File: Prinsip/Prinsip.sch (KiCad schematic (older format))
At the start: 21 parts

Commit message: One element
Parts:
- removed U? (x7): 7451N, symbol Prinsip:7451N
- removed U? (x7): 7426N, symbol Prinsip:7426N
- added U? (x2): 7426N, symbol Prinsip:7426N
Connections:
- wire segments 0 -> 9
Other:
- moved on the sheet: U?A

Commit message: Optimized
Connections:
- wire segments 9 -> 11
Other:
- moved on the sheet: U?A
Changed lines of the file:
@@
 L Prinsip:7420N U?
 U 1 1 61669E61
-P 8100 3100
-F 0 "U?" H 8075 3566 50  0000 C CNN
-F 1 "7420N" H 8075 3475 50  0000 C CNN
-F 2 "" H 8100 3250 50  0001 C CNN
-F 3 "" H 8100 3250 50  0001 C CNN
-	1    8100 3100
+P 10750 3050
+F 0 "U?" H 10725 3516 50  0000 C CNN
+F 1 "7420N" H 10725 3425 50  0000 C CNN
+F 2 "" H 10750 3200 50  0001 C CNN
+F 3 "" H 10750 3200 50  0001 C CNN
+	1    10750 3050
 	1    0    0    -1
 $EndComp
@@
 L Prinsip:7420N U?
 U 1 1 6166CDF9
-P 8100 7000
-F 0 "U?" H 8075 7466 50  0000 C CNN
-F 1 "7420N" H 8075 7375 50  0000 C CNN
-F 2 "" H 8100 7150 50  0001 C CNN
-F 3 "" H 8100 7150 50  0001 C CNN
-	1    8100 7000
+P 10750 6950
+F 0 "U?" H 10725 7416 50  0000 C CNN
+F 1 "7420N" H 10725 7325 50  0000 C CNN
+F 2 "" H 10750 7100 50  0001 C CNN
+F 3 "" H 10750 7100 50  0001 C CNN
+	1    10750 6950
 	1    0    0    -1
 $EndComp
@@
 L Prinsip:7426N U?
 U 1 1 6166FCF7
-P 9450 3950
-F 0 "U?" H 9450 4416 50  0000 C CNN
-F 1 "7426N" H 9450 4325 50  0000 C CNN
-F 2 "" H 9450 4100 50  0001 C CNN
-F 3 "" H 9450 4100 50  0001 C CNN
-	1    9450 3950
+P 12100 3900
+F 0 "U?" H 12100 4366 50  0000 C CNN
+F 1 "7426N" H 12100 4275 50  0000 C CNN
+F 2 "" H 12100 4050 50  0001 C CNN
+F 3 "" H 12100 4050 50  0001 C CNN
+	1    12100 3900
 	1    0    0    -1
 $EndComp
@@
 L Prinsip:7426N U?
 U 1 1 61671269
-P 9450 5900
-F 0 "U?" H 9450 6366 50  0000 C CNN
-F 1 "7426N" H 9450 6275 50  0000 C CNN
-F 2 "" H 9450 6050 50  0001 C CNN
-F 3 "" H 9450 6050 50  0001 C CNN
-	1    9450 5900
+P 12100 5850
+F 0 "U?" H 12100 6316 50  0000 C CNN
+F 1 "7426N" H 12100 6225 50  0000 C CNN
+F 2 "" H 12100 6000 50  0001 C CNN
+F 3 "" H 12100 6000 50  0001 C CNN
+	1    12100 5850
 	1    0    0    -1
 $EndComp
@@
 L Prinsip:7426N U?
 U 1 1 61671C84
-P 10950 4900
-F 0 "U?" H 10950 5366 50  0000 C CNN
-F 1 "7426N" H 10950 5275 50  0000 C CNN
-F 2 "" H 10950 5050 50  0001 C CNN
-F 3 "" H 10950 5050 50  0001 C CNN
-	1    10950 4900
-	1    0    0    -1
-$EndComp
-$Comp
-L Prinsip:7426N U?
-U 1 1 6166AF0B
-P 3500 3000
-F 0 "U?" H 3500 3466 50  0000 C CNN
-F 1 "7426N" H 3500 3375 50  0000 C CNN
-F 2 "" H 3500 3150 50  0001 C CNN
-F 3 "" H 3500 3150 50  0001 C CNN
-	1    3500 3000
+P 13600 4850
+F 0 "U?" H 13600 5316 50  0000 C CNN
+F 1 "7426N" H 13600 5225 50  0000 C CNN
+F 2 "" H 13600 5000 50  0001 C CNN
+F 3 "" H 13600 5000 50  0001 C CNN
+	1    13600 4850
 	1    0    0    -1
 $EndComp
@@
 L Prinsip:7426N U?
 U 1 1 6166A9DA
-P 3500 2200
-F 0 "U?" H 3500 2666 50  0000 C CNN
-F 1 "7426N" H 3500 2575 50  0000 C CNN
-F 2 "" H 3500 2350 50  0001 C CNN
-F 3 "" H 3500 2350 50  0001 C CNN
-	1    3500 2200
+P 2350 1700
+F 0 "U?" H 2350 2166 50  0000 C CNN
+F 1 "7426N" H 2350 2075 50  0000 C CNN
+F 2 "" H 2350 1850 50  0001 C CNN
+F 3 "" H 2350 1850 50  0001 C CNN
+	1    2350 1700
 	1    0    0    -1
 $EndComp
 Wire Wire Line
-	4400 1700 4000 1700
-Wire Wire Line
-	4000 1700 4000 2200
-Wire Wire Line
 	4400 1800 4100 1800
-Wire Wire Line
-	4100 1800 4100 3000
-Wire Wire Line
-	4100 3000 4000 3000
 $Comp
 L Prinsip:7426N U?
@@
 Wire Wire Line
 	5650 1650 5650 1750
+Wire Wire Line
+	4400 1500 2600 1500
+Wire Wire Line
+	2850 1700 4400 1700
+Wire Wire Line
+	4100 2800 4000 2800
+$Comp
+L Prinsip:7426N U?
+U 1 1 6166AF0B
+P 3500 2800
+F 0 "U?" H 3500 3266 50  0000 C CNN
+F 1 "7426N" H 3500 3175 50  0000 C CNN
+F 2 "" H 3500 2950 50  0001 C CNN
+F 3 "" H 3500 2950 50  0001 C CNN
+	1    3500 2800
+	1    0    0    -1
+$EndComp
+Wire Wire Line
+	3000 2700 3000 2800
+Wire Wire Line
+	2800 2800 3000 2800
+Connection ~ 3000 2800
+Wire Wire Line
+	3000 2800 3000 2900
 $EndSCHEMATC

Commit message: 7451 placement
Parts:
- added U? (x7): 7451N, symbol Prinsip:7451N
- added U? (x21): 7426N, symbol Prinsip:7426N
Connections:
- wire segments 11 -> 136
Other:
- moved on the sheet: U?A

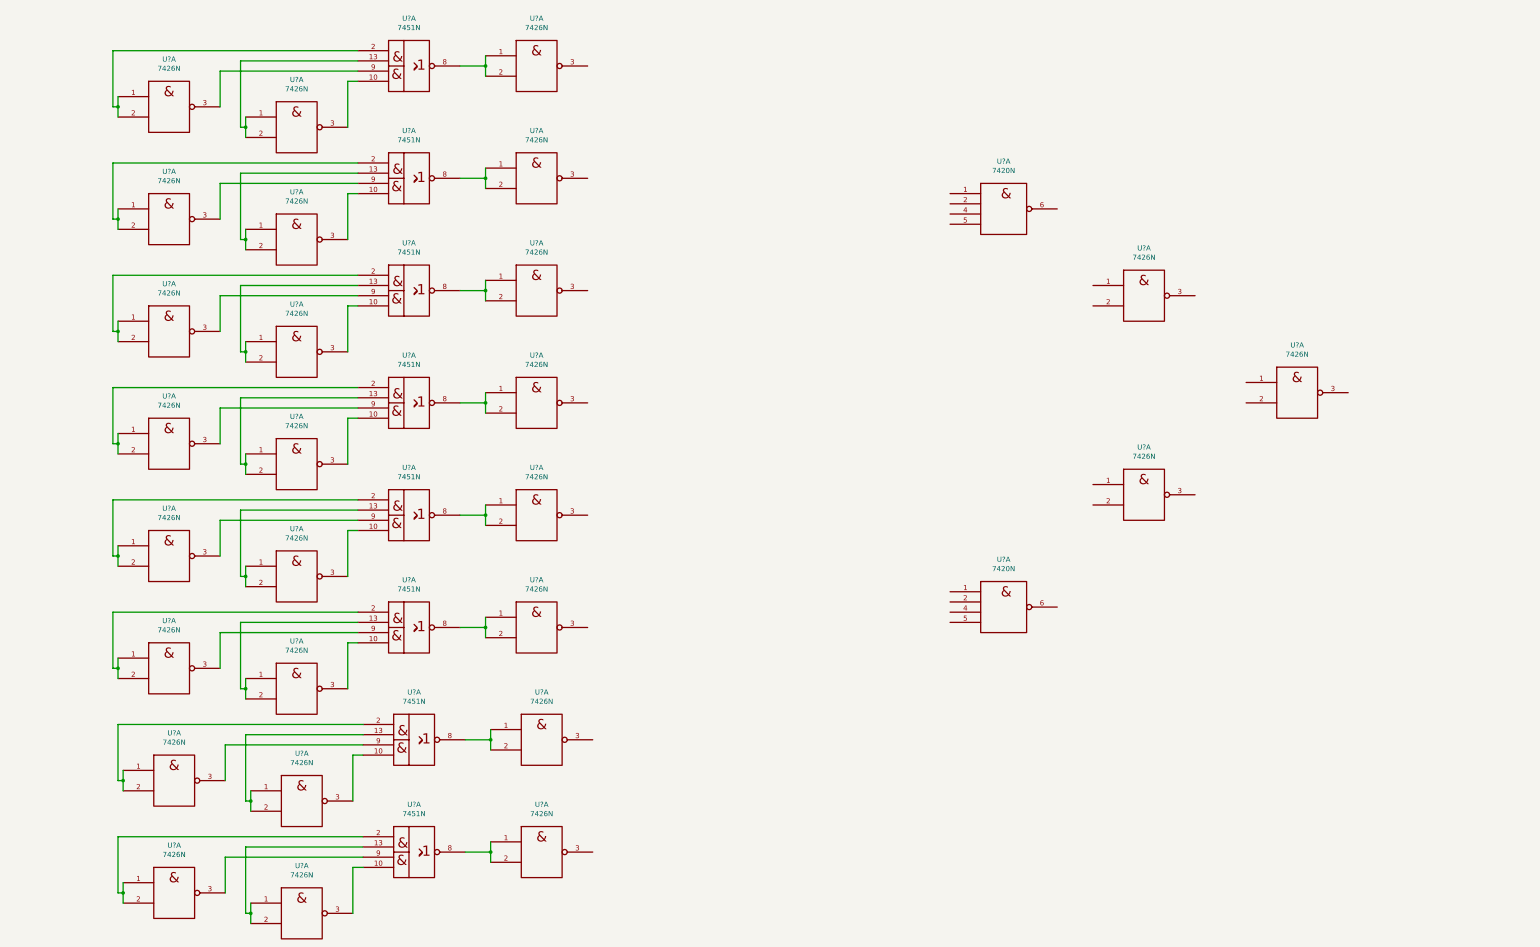
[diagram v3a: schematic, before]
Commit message: 7426N placement
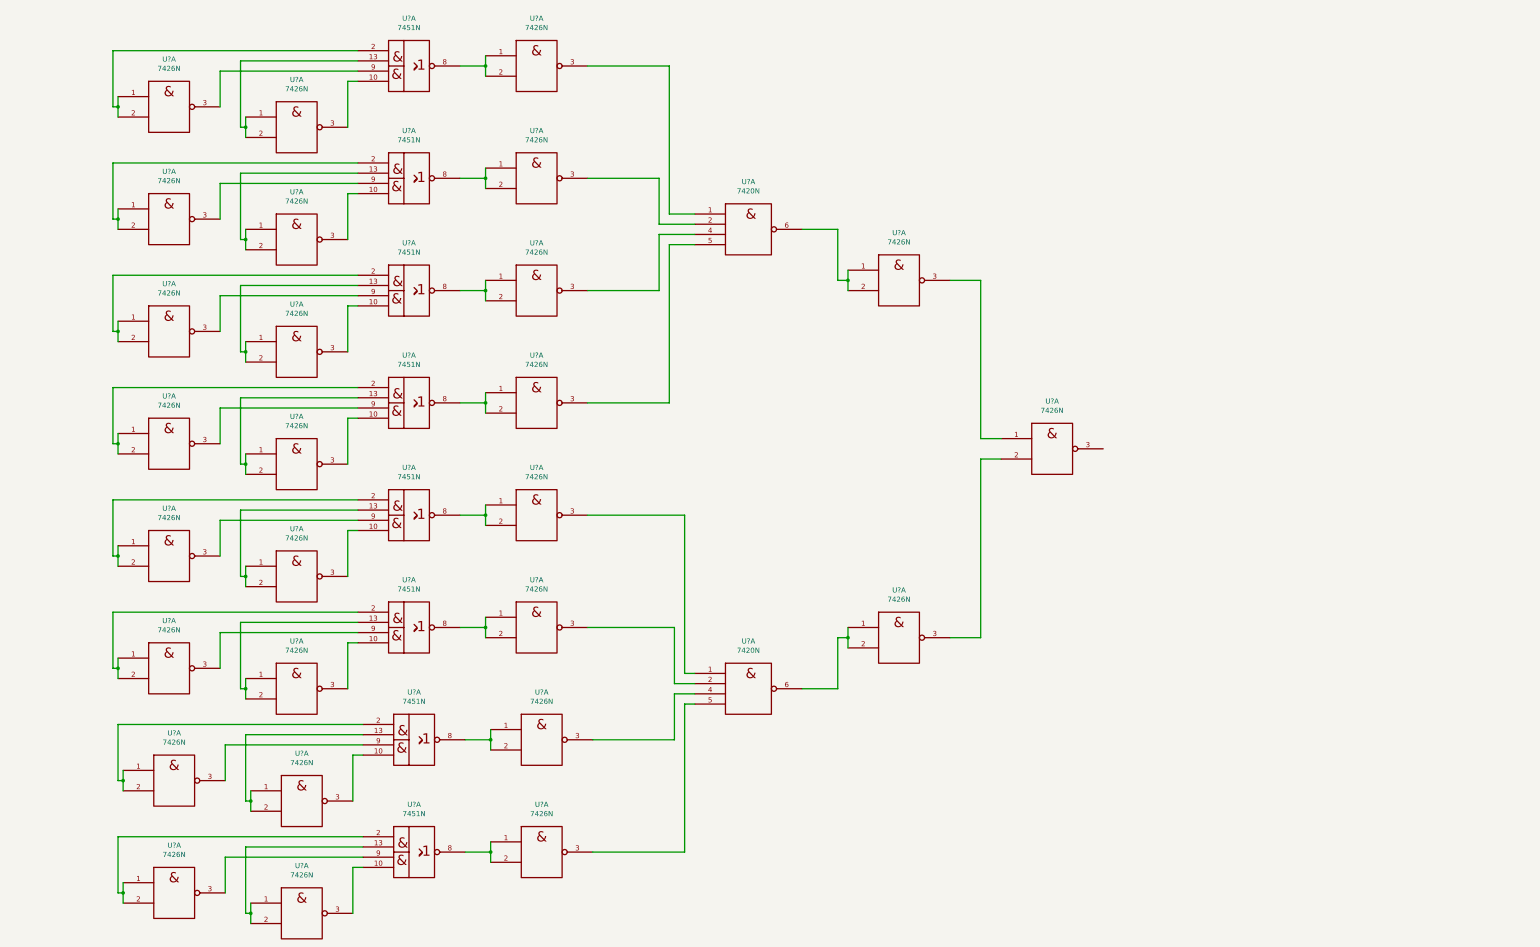
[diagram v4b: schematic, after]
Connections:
- net at U?.3: now also U?.1 (x2)
- net at U?.2: now also U?.3 (x2)
- net at U?.4: now also U?.3 (x2)
- net at U?.5: now also U?.3 (x2)
- net at U?.6: now also U?.1, U?.2 (x2)
- net at U?.1: now also U?.3
- net at U?.3: now also U?.2
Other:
- moved on the sheet: U?A
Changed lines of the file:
@@
 L Prinsip:7420N U?
 U 1 1 61669E61
-P 10750 3050
-F 0 "U?" H 10725 3516 50  0000 C CNN
-F 1 "7420N" H 10725 3425 50  0000 C CNN
-F 2 "" H 10750 3200 50  0001 C CNN
-F 3 "" H 10750 3200 50  0001 C CNN
-	1    10750 3050
+P 8250 3250
+F 0 "U?" H 8225 3716 50  0000 C CNN
+F 1 "7420N" H 8225 3625 50  0000 C CNN
+F 2 "" H 8250 3400 50  0001 C CNN
+F 3 "" H 8250 3400 50  0001 C CNN
+	1    8250 3250
 	1    0    0    -1
 $EndComp
@@
 L Prinsip:7420N U?
 U 1 1 6166CDF9
-P 10750 6950
-F 0 "U?" H 10725 7416 50  0000 C CNN
-F 1 "7420N" H 10725 7325 50  0000 C CNN
-F 2 "" H 10750 7100 50  0001 C CNN
-F 3 "" H 10750 7100 50  0001 C CNN
-	1    10750 6950
+P 8250 7750
+F 0 "U?" H 8225 8216 50  0000 C CNN
+F 1 "7420N" H 8225 8125 50  0000 C CNN
+F 2 "" H 8250 7900 50  0001 C CNN
+F 3 "" H 8250 7900 50  0001 C CNN
+	1    8250 7750
 	1    0    0    -1
 $EndComp
@@
 L Prinsip:7426N U?
 U 1 1 6166FCF7
-P 12100 3900
-F 0 "U?" H 12100 4366 50  0000 C CNN
-F 1 "7426N" H 12100 4275 50  0000 C CNN
-F 2 "" H 12100 4050 50  0001 C CNN
-F 3 "" H 12100 4050 50  0001 C CNN
-	1    12100 3900
+P 9700 3750
+F 0 "U?" H 9700 4216 50  0000 C CNN
+F 1 "7426N" H 9700 4125 50  0000 C CNN
+F 2 "" H 9700 3900 50  0001 C CNN
+F 3 "" H 9700 3900 50  0001 C CNN
+	1    9700 3750
 	1    0    0    -1
 $EndComp
@@
 L Prinsip:7426N U?
 U 1 1 61671269
-P 12100 5850
-F 0 "U?" H 12100 6316 50  0000 C CNN
-F 1 "7426N" H 12100 6225 50  0000 C CNN
-F 2 "" H 12100 6000 50  0001 C CNN
-F 3 "" H 12100 6000 50  0001 C CNN
-	1    12100 5850
+P 9700 7250
+F 0 "U?" H 9700 7716 50  0000 C CNN
+F 1 "7426N" H 9700 7625 50  0000 C CNN
+F 2 "" H 9700 7400 50  0001 C CNN
+F 3 "" H 9700 7400 50  0001 C CNN
+	1    9700 7250
 	1    0    0    -1
 $EndComp
@@
 L Prinsip:7426N U?
 U 1 1 61671C84
-P 13600 4850
-F 0 "U?" H 13600 5316 50  0000 C CNN
-F 1 "7426N" H 13600 5225 50  0000 C CNN
-F 2 "" H 13600 5000 50  0001 C CNN
-F 3 "" H 13600 5000 50  0001 C CNN
-	1    13600 4850
+P 11200 5400
+F 0 "U?" H 11200 5866 50  0000 C CNN
+F 1 "7426N" H 11200 5775 50  0000 C CNN
+F 2 "" H 11200 5550 50  0001 C CNN
+F 3 "" H 11200 5550 50  0001 C CNN
+	1    11200 5400
 	1    0    0    -1
 $EndComp
@@
 Wire Wire Line
 	3350 9950 3350 10050
+Wire Wire Line
+	6650 1650 7450 1650
+Wire Wire Line
+	7450 1650 7450 3100
+Wire Wire Line
+	7450 3100 7700 3100
+Wire Wire Line
+	6650 2750 7350 2750
+Wire Wire Line
+	7350 2750 7350 3200
+Wire Wire Line
+	7350 3200 7700 3200
+Wire Wire Line
+	6650 3850 7350 3850
+Wire Wire Line
+	7350 3850 7350 3300
+Wire Wire Line
+	7350 3300 7700 3300
+Wire Wire Line
+	7700 3400 7450 3400
+Wire Wire Line
+	7450 3400 7450 4950
+Wire Wire Line
+	7450 4950 6650 4950
+Wire Wire Line
+	6650 6050 7600 6050
+Wire Wire Line
+	7600 6050 7600 7600
+Wire Wire Line
+	7600 7600 7700 7600
+Wire Wire Line
+	6650 7150 7500 7150
+Wire Wire Line
+	7500 7150 7500 7700
+Wire Wire Line
+	7500 7700 7700 7700
+Wire Wire Line
+	6700 8250 7500 8250
+Wire Wire Line
+	7500 8250 7500 7800
+Wire Wire Line
+	7500 7800 7700 7800
+Wire Wire Line
+	6700 9350 7600 9350
+Wire Wire Line
+	7600 9350 7600 7900
+Wire Wire Line
+	7600 7900 7700 7900
+Wire Wire Line
+	9200 7150 9200 7250
+Wire Wire Line
+	8750 7750 9100 7750
+Wire Wire Line
+	9100 7750 9100 7250
+Wire Wire Line
+	9100 7250 9200 7250
+Connection ~ 9200 7250
+Wire Wire Line
+	9200 7250 9200 7350
+Wire Wire Line
+	9200 3650 9200 3750
+Wire Wire Line
+	8750 3250 9100 3250
+Wire Wire Line
+	9100 3250 9100 3750
+Wire Wire Line
+	9100 3750 9200 3750
+Connection ~ 9200 3750
+Wire Wire Line
+	9200 3750 9200 3850
+Wire Wire Line
+	10200 3750 10500 3750
+Wire Wire Line
+	10200 7250 10500 7250
+Wire Wire Line
+	10500 3750 10500 5300
+Wire Wire Line
+	10500 5300 10700 5300
+Wire Wire Line
+	10500 7250 10500 5500
+Wire Wire Line
+	10500 5500 10700 5500
 $EndSCHEMATC

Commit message: General alignment
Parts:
- removed U?: 7420N, symbol Prinsip:7420N
- added U?: 7420N, symbol Prinsip:7420N
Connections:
- net Gnd: now also U?.7 (Gnd)
- net Vcc: now also U?.14 (Vcc)
- net at U?.3: now also U?.1
- net at U?.3: now also U?.2
- net at U?.3: now also U?.4
- net at U?.3: now also U?.5
- net at U?.1, U?.2: now also U?.6
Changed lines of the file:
@@
-$Comp
-L Prinsip:7420N U?
-U 1 1 61669E61
-P 8250 3250
-F 0 "U?" H 8225 3716 50  0000 C CNN
-F 1 "7420N" H 8225 3625 50  0000 C CNN
-F 2 "" H 8250 3400 50  0001 C CNN
-F 3 "" H 8250 3400 50  0001 C CNN
-	1    8250 3250
-	1    0    0    -1
-$EndComp
 $Comp
 L Prinsip:7420N U?
@@
 $Comp
 L Prinsip:7426N U?
-U 1 1 6166FCF7
-P 9700 3750
-F 0 "U?" H 9700 4216 50  0000 C CNN
-F 1 "7426N" H 9700 4125 50  0000 C CNN
-F 2 "" H 9700 3900 50  0001 C CNN
-F 3 "" H 9700 3900 50  0001 C CNN
-	1    9700 3750
-	1    0    0    -1
-$EndComp
-$Comp
-L Prinsip:7426N U?
 U 1 1 61671269
 P 9700 7250
@@
 F 3 "" H 11200 5550 50  0001 C CNN
 	1    11200 5400
-	1    0    0    -1
-$EndComp
-$Comp
-L Prinsip:7426N U?
-U 1 1 61665BB4
-P 6150 1650
-F 0 "U?" H 6150 2116 50  0000 C CNN
-F 1 "7426N" H 6150 2025 50  0000 C CNN
-F 2 "" H 6150 1800 50  0001 C CNN
-F 3 "" H 6150 1800 50  0001 C CNN
-	1    6150 1650
 	1    0    0    -1
 $EndComp
@@
 	1    0    0    -1
 $EndComp
-$Comp
-L Prinsip:7426N U?
-U 1 1 61672D4B
-P 6150 2750
-F 0 "U?" H 6150 3216 50  0000 C CNN
-F 1 "7426N" H 6150 3125 50  0000 C CNN
-F 2 "" H 6150 2900 50  0001 C CNN
-F 3 "" H 6150 2900 50  0001 C CNN
-	1    6150 2750
-	1    0    0    -1
-$EndComp
 Wire Wire Line
 	5650 2650 5650 2750
@@
 	1    0    0    -1
 $EndComp
-$Comp
-L Prinsip:7426N U?
-U 1 1 61675E65
-P 6150 3850
-F 0 "U?" H 6150 4316 50  0000 C CNN
-F 1 "7426N" H 6150 4225 50  0000 C CNN
-F 2 "" H 6150 4000 50  0001 C CNN
-F 3 "" H 6150 4000 50  0001 C CNN
-	1    6150 3850
-	1    0    0    -1
-$EndComp
 Wire Wire Line
 	5650 3750 5650 3850
@@
 	1    0    0    -1
 $EndComp
-$Comp
-L Prinsip:7426N U?
-U 1 1 61684585
-P 6150 4950
-F 0 "U?" H 6150 5416 50  0000 C CNN
-F 1 "7426N" H 6150 5325 50  0000 C CNN
-F 2 "" H 6150 5100 50  0001 C CNN
-F 3 "" H 6150 5100 50  0001 C CNN
-	1    6150 4950
-	1    0    0    -1
-$EndComp
 Wire Wire Line
 	5650 4850 5650 4950
@@
 	3350 9950 3350 10050
 Wire Wire Line
-	6650 1650 7450 1650
-Wire Wire Line
-	7450 1650 7450 3100
-Wire Wire Line
-	7450 3100 7700 3100
-Wire Wire Line
-	6650 2750 7350 2750
-Wire Wire Line
-	7350 2750 7350 3200
-Wire Wire Line
-	7350 3200 7700 3200
-Wire Wire Line
-	6650 3850 7350 3850
-Wire Wire Line
-	7350 3850 7350 3300
-Wire Wire Line
-	7350 3300 7700 3300
-Wire Wire Line
-	7700 3400 7450 3400
-Wire Wire Line
-	7450 3400 7450 4950
-Wire Wire Line
-	7450 4950 6650 4950
-Wire Wire Line
-	6650 6050 7600 6050
-Wire Wire Line
-	7600 6050 7600 7600
-Wire Wire Line
-	7600 7600 7700 7600
-Wire Wire Line
-	6650 7150 7500 7150
-Wire Wire Line
-	7500 7150 7500 7700
-Wire Wire Line
-	7500 7700 7700 7700
-Wire Wire Line
-	6700 8250 7500 8250
-Wire Wire Line
-	7500 8250 7500 7800
-Wire Wire Line
-	7500 7800 7700 7800
-Wire Wire Line
-	6700 9350 7600 9350
-Wire Wire Line
-	7600 9350 7600 7900
-Wire Wire Line
-	7600 7900 7700 7900
+	7500 9350 7500 7900
+Wire Wire Line
+	10200 3750 10500 3750
+Wire Wire Line
+	10200 7250 10500 7250
+Wire Wire Line
+	10500 3750 10500 5300
+Wire Wire Line
+	10500 5300 10700 5300
+Wire Wire Line
+	10500 7250 10500 5500
+Wire Wire Line
+	10500 5500 10700 5500
+Wire Wire Line
+	6700 9350 7500 9350
+Wire Wire Line
+	7500 7900 7700 7900
+Wire Wire Line
+	7000 7800 7000 8250
+Wire Wire Line
+	7000 8250 6700 8250
+Wire Wire Line
+	7000 7800 7700 7800
+Wire Wire Line
+	7500 7600 7700 7600
+Wire Wire Line
+	6650 6050 7500 6050
+Wire Wire Line
+	7500 6050 7500 7600
+Wire Wire Line
+	7700 7700 7000 7700
+Wire Wire Line
+	7000 7700 7000 7150
+Wire Wire Line
+	7000 7150 6650 7150
+$Comp
+L Prinsip:7426N U?
+U 1 1 61684585
+P 6150 4950
+F 0 "U?" H 6150 5416 50  0000 C CNN
+F 1 "7426N" H 6150 5325 50  0000 C CNN
+F 2 "" H 6150 5100 50  0001 C CNN
+F 3 "" H 6150 5100 50  0001 C CNN
+	1    6150 4950
+	1    0    0    -1
+$EndComp
+$Comp
+L Prinsip:7426N U?
+U 1 1 61675E65
+P 6150 3850
+F 0 "U?" H 6150 4316 50  0000 C CNN
+F 1 "7426N" H 6150 4225 50  0000 C CNN
+F 2 "" H 6150 4000 50  0001 C CNN
+F 3 "" H 6150 4000 50  0001 C CNN
+	1    6150 3850
+	1    0    0    -1
+$EndComp
+$Comp
+L Prinsip:7426N U?
+U 1 1 61672D4B
+P 6150 2750
+F 0 "U?" H 6150 3216 50  0000 C CNN
+F 1 "7426N" H 6150 3125 50  0000 C CNN
+F 2 "" H 6150 2900 50  0001 C CNN
+F 3 "" H 6150 2900 50  0001 C CNN
+	1    6150 2750
+	1    0    0    -1
+$EndComp
+$Comp
+L Prinsip:7426N U?
+U 1 1 61665BB4
+P 6150 1650
+F 0 "U?" H 6150 2116 50  0000 C CNN
+F 1 "7426N" H 6150 2025 50  0000 C CNN
+F 2 "" H 6150 1800 50  0001 C CNN
+F 3 "" H 6150 1800 50  0001 C CNN
+	1    6150 1650
+	1    0    0    -1
+$EndComp
+$Comp
+L Prinsip:7420N U?
+U 1 1 61810D02
+P 8250 3350
+F 0 "U?" H 8225 3816 50  0000 C CNN
+F 1 "7420N" H 8225 3725 50  0000 C CNN
+F 2 "" H 8250 3500 50  0001 C CNN
+F 3 "" H 8250 3500 50  0001 C CNN
+	1    8250 3350
+	1    0    0    -1
+$EndComp
+Wire Wire Line
+	7500 4950 7500 3500
+Wire Wire Line
+	7500 3500 7700 3500
+Wire Wire Line
+	7000 3400 7000 3850
+Wire Wire Line
+	7000 3400 7700 3400
+Wire Wire Line
+	7500 3200 7700 3200
+Wire Wire Line
+	6650 1650 7500 1650
+Wire Wire Line
+	7500 1650 7500 3200
+Wire Wire Line
+	7700 3300 7000 3300
+Wire Wire Line
+	7000 3300 7000 2750
+Wire Wire Line
+	7000 2750 6650 2750
+$Comp
+L Prinsip:7426N U?
+U 1 1 6166FCF7
+P 9700 3750
+F 0 "U?" H 9700 4216 50  0000 C CNN
+F 1 "7426N" H 9700 4125 50  0000 C CNN
+F 2 "" H 9700 3900 50  0001 C CNN
+F 3 "" H 9700 3900 50  0001 C CNN
+	1    9700 3750
+	1    0    0    -1
+$EndComp
+Wire Wire Line
+	9200 3650 9200 3750
+Wire Wire Line
+	8750 3350 9000 3350
+Wire Wire Line
+	9000 3350 9000 3750
+Wire Wire Line
+	9000 3750 9200 3750
+Connection ~ 9200 3750
+Wire Wire Line
+	9200 3750 9200 3850
 Wire Wire Line
 	9200 7150 9200 7250
 Wire Wire Line
-	8750 7750 9100 7750
-Wire Wire Line
-	9100 7750 9100 7250
-Wire Wire Line
-	9100 7250 9200 7250
+	8750 7750 9000 7750
+Wire Wire Line
+	9000 7750 9000 7250
+Wire Wire Line
+	9000 7250 9200 7250
 Connection ~ 9200 7250
 Wire Wire Line
 	9200 7250 9200 7350
 Wire Wire Line
-	9200 3650 9200 3750
-Wire Wire Line
-	8750 3250 9100 3250
-Wire Wire Line
-	9100 3250 9100 3750
-Wire Wire Line
-	9100 3750 9200 3750
-Connection ~ 9200 3750
-Wire Wire Line
-	9200 3750 9200 3850
-Wire Wire Line
-	10200 3750 10500 3750
-Wire Wire Line
-	10200 7250 10500 7250
-Wire Wire Line
-	10500 3750 10500 5300
-Wire Wire Line
-	10500 5300 10700 5300
-Wire Wire Line
-	10500 7250 10500 5500
-Wire Wire Line
-	10500 5500 10700 5500
+	6650 3850 7000 3850
+Wire Wire Line
+	6650 4950 7500 4950
 $EndSCHEMATC

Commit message: Updated
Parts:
- added SW?: SW_DIP_x08, symbol Switch:SW_DIP_x08
- added U?: DAC, symbol Prinsip:DAC
- added U?: 74199N, symbol Prinsip:74199N
- added U?: COUNTER, symbol Prinsip:COUNTER
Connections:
- net CT: now reaches U?.1, U?.13, U?.2
- net CT: now also U?.~ (~LD), U?.~ (~LOAD)
- net at U?.1, U?.2, U?.2: now also SW?.16
- net at U?.3: now also U?.~ (~LOAD)
- net CT1: now reaches U?.1, U?.13, U?.2
- net CT1: now also U?.~ (~LD), U?.~ (~LOAD)
- net at U?.1, U?.2, U?.2: now also SW?.15
- net CT2: now reaches U?.1, U?.13, U?.2
- net CT2: now also U?.~ (~LD), U?.~ (~LOAD)
- net at U?.1, U?.2, U?.2: now also SW?.14
- net CT3: now reaches U?.1, U?.13, U?.2
- net CT3: now also U?.~ (~LD), U?.~ (~LOAD)
- net at U?.1, U?.2, U?.2: now also SW?.13
- net CT4: now reaches U?.1, U?.13, U?.2
- net CT4: now also U?.~ (~LD), U?.~ (~LOAD)
- net at U?.1, U?.2, U?.2: now also SW?.12
- net CT5: now reaches U?.1, U?.13, U?.2
- net CT5: now also U?.~ (~LD), U?.~ (~LOAD)
- net at U?.1, U?.2, U?.2: now also SW?.11
- net CT6: now reaches U?.1, U?.13, U?.2
- net CT6: now also U?.~ (~LD), U?.~ (~LOAD)
- net at U?.1, U?.2, U?.2: now also SW?.10
- net CT7: now reaches U?.1, U?.13, U?.2
- net CT7: now also U?.~ (~LD), U?.~ (~LOAD)
- net at U?.1, U?.2, U?.2: now also SW?.9
- new net: U?.~ (Uоп), U?.~ (~LD) (x8)
- new net +24V: U?.~ (Uоп)
- new net +5V: SW?.1, SW?.2, SW?.3, SW?.4, SW?.5, SW?.6, SW?.7, SW?.8
- new net CLK: U?.~ (~LD), U?.~ (~LOAD)
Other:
- moved on the sheet: U?A

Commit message: Updated Prinsip
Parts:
- added DD38: 7404, symbol 74xx_IEEE:7404
- added R1, R2: R_Small-Device, symbol Принципиально-rescue:R_Small-Device
- added U?: TAB-Prinsip, symbol Принципиально-rescue:TAB-Prinsip
- added ZQ1: Resonator-Device, symbol Принципиально-rescue:Resonator-Device
- DD39: renamed from U?; value COUNTER -> 74160N
- gave numbers to parts that had none: 39
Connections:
- net CLK: now also DD38.2, R1.2, R2.1
- net Gnd: now also DD38.7 (Gnd)
- net Vcc: now also DD38.14 (Vcc)
- new net: DD38.1, R1.1, ZQ1.1
- new net: R2.2, ZQ1.3
- new net: DD40.~ (~LD), DD41.~ (Uоп) (x8)
- new net Earth: ZQ1.2
